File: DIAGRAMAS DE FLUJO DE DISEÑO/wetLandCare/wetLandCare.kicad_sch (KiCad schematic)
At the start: 9 parts, among them M1 Motor_DC, M2 Motor_DC, U1 ESP32-CAM, U2 L298N, U3 AMS1117-5.0, U4 AMS1117-3.3, U5 L298N

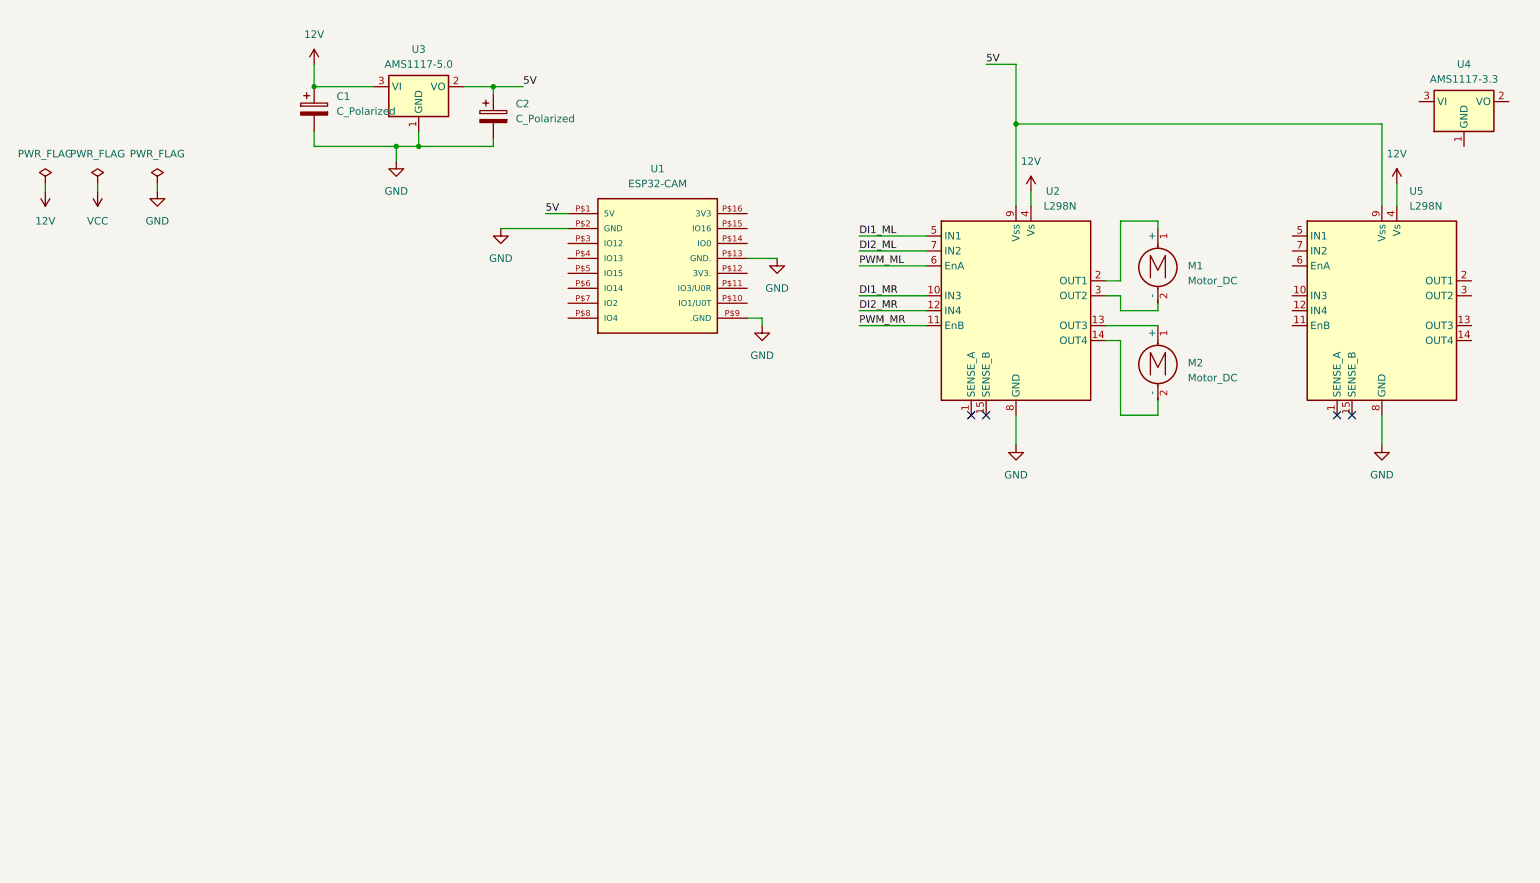
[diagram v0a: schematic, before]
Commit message: Add files via upload
Modificación y complementación del diagrama esquemático como parte del diseño técnico del prototipo
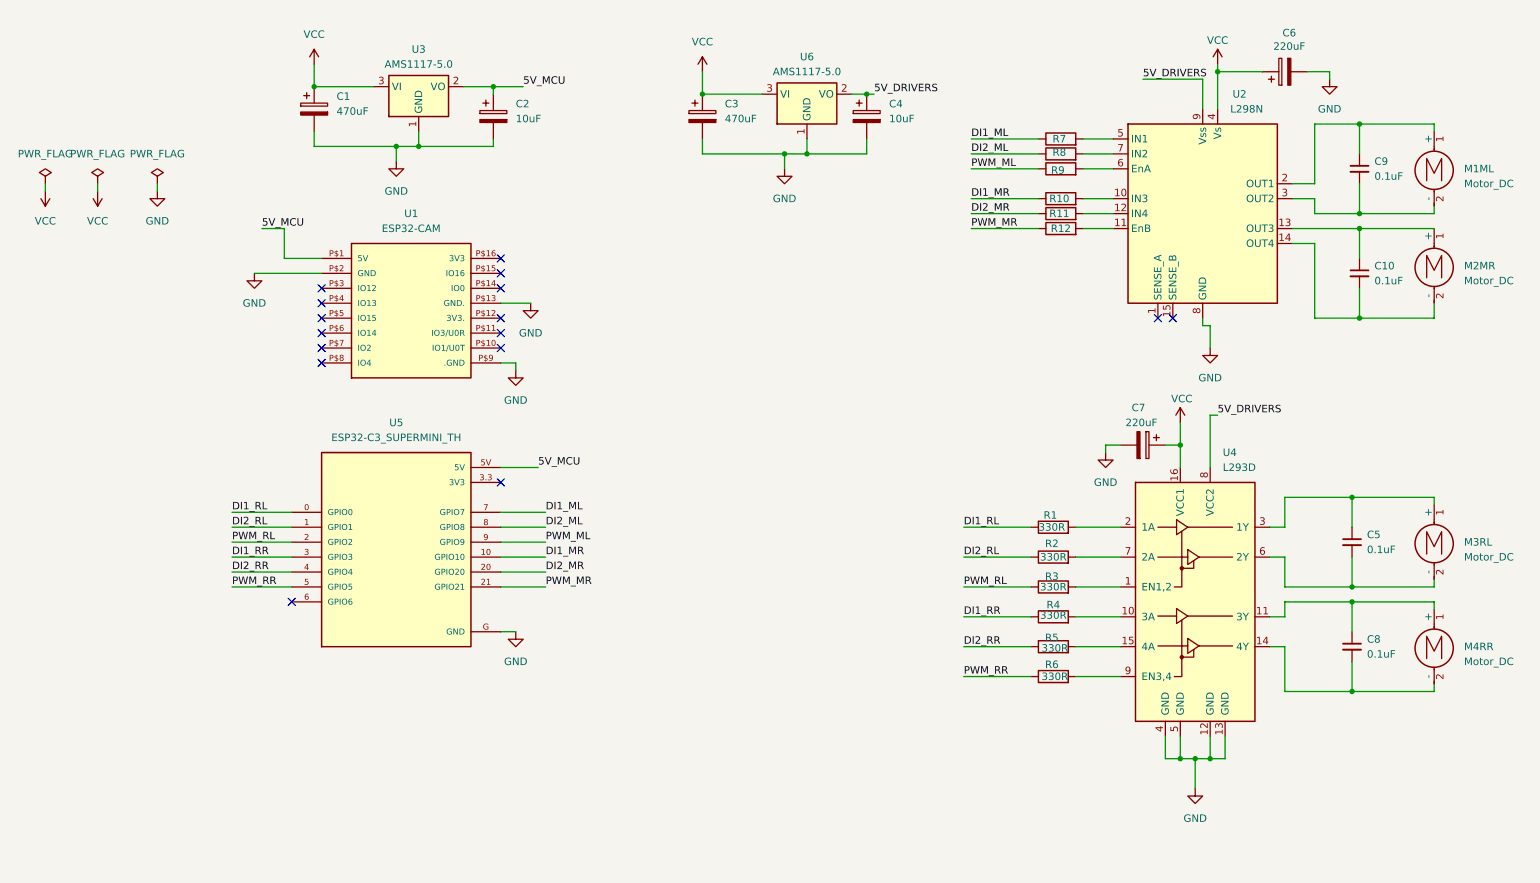
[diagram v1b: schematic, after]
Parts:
- removed U4: AMS1117-3.3, Package_TO_SOT_SMD:SOT-223-3_TabPin2, symbol Regulator_Linear:AMS1117-3.3
- removed U5: L298N, Package_TO_SOT_THT:TO-220-15_P2.54x5.08mm_StaggerOdd_Lead4.58mm_Vertical, symbol Driver_Motor:L298N
- added C10, C5, C8, C9: 0.1uF, symbol Device:C_Small
- added C3: 470uF, symbol Device:C_Polarized
- added C4: 10uF, symbol Device:C_Polarized
- added C6, C7: 220uF, symbol Device:C_Polarized
- added M3RL, M4RR: Motor_DC, symbol Motor:Motor_DC
- added R1, R10, R11, R12, R2, R3, R4, R5, R6, R7, R8, R9: 330R, symbol Device:R
- added U4: L293D, Package_DIP:DIP-16_W7.62mm, symbol Driver_Motor:L293D
- added U5: ESP32-C3_SUPERMINI_TH, ESP32 C3 SuperMini:MODULE_ESP32-C3_SUPERMINI_TH, symbol ESP32-C3_SUPERMINI_TH:ESP32-C3_SUPERMINI_TH
- added U6: AMS1117-5.0, Package_TO_SOT_SMD:SOT-223-3_TabPin2, symbol Regulator_Linear:AMS1117-5.0
- C1: value C_Polarized -> 470uF
- C2: value C_Polarized -> 10uF
- U1: footprint ESP32-CAM:ESP32-CAM -> ESP32CAM:ESP32-CAM
- renumbered M1 to M1ML, M2 to M2MR
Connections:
- net 12V is gone; now on net VCC: C1.1, U2.4 (Vs), U3.3 (VI)
- net DI1_ML: now also R7.1, U5.7 (GPIO7); no longer U2.5 (IN1)
- net DI1_MR: now also R10.1, U5.10 (GPIO10); no longer U2.10 (IN3)
- net DI2_ML: now also R8.1, U5.8 (GPIO8); no longer U2.7 (IN2)
- net DI2_MR: now also R11.1, U5.20 (GPIO20); no longer U2.12 (IN4)
- net GND: now also C3.2, C4.2, C6.2, C7.2, U4.12 (GND), U4.13 (GND), U4.4 (GND), U4.5 (GND), U5.G (GND), U6.1 (GND)
- net PWM_ML: now also R9.1, U5.9 (GPIO9); no longer U2.6 (EnA)
- net PWM_MR: now also R12.1, U5.21 (GPIO21); no longer U2.11 (EnB)
- net VCC: now also C3.1, C6.1, C7.1, U4.16 (VCC1), U6.3 (VI)
- net at M1ML.1 (+), U2.2 (OUT1): now also C9.1
- net at M1ML.2 (-), U2.3 (OUT2): now also C9.2
- net at M2MR.1 (+), U2.13 (OUT3): now also C10.1
- net at M2MR.2 (-), U2.14 (OUT4): now also C10.2
- net 5V renamed 5V_MCU
- net 5V_MCU: now also U5.5V; no longer U2.9 (Vss)
- new net: R6.2, U4.9 (EN3,4)
- new net: R9.2, U2.6 (EnA)
- new net: R3.2, U4.1 (EN1,2)
- new net: R4.2, U4.10 (3A)
- new net: C8.1, M4RR.1 (+), U4.11 (3Y)
- new net: C8.2, M4RR.2 (-), U4.14 (4Y)
- new net: R5.2, U4.15 (4A)
- new net: R1.2, U4.2 (1A)
- new net: C5.1, M3RL.1 (+), U4.3 (1Y)
- new net: C5.2, M3RL.2 (-), U4.6 (2Y)
- new net: R2.2, U4.7 (2A)
- new net: R7.2, U2.5 (IN1)
- new net: R10.2, U2.10 (IN3)
- new net: R11.2, U2.12 (IN4)
- new net: R12.2, U2.11 (EnB)
- new net: R8.2, U2.7 (IN2)
- new net 5V_DRIVERS: C4.1, U2.9 (Vss), U4.8 (VCC2), U6.2 (VO)
- new net DI1_RL: R1.1, U5.0 (GPIO0)
- new net DI1_RR: R4.1, U5.3 (GPIO3)
- new net DI2_RL: R2.1, U5.1 (GPIO1)
- new net DI2_RR: R5.1, U5.4 (GPIO4)
- new net PWM_RL: R3.1, U5.2 (GPIO2)
- new net PWM_RR: R6.1, U5.5 (GPIO5)
- no-connect marks 4 -> 16
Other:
- moved on the sheet: M1ML, M2MR, U1, U2

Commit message: added via upload
Modificaciones al esquemático y diseño del circuito impreso
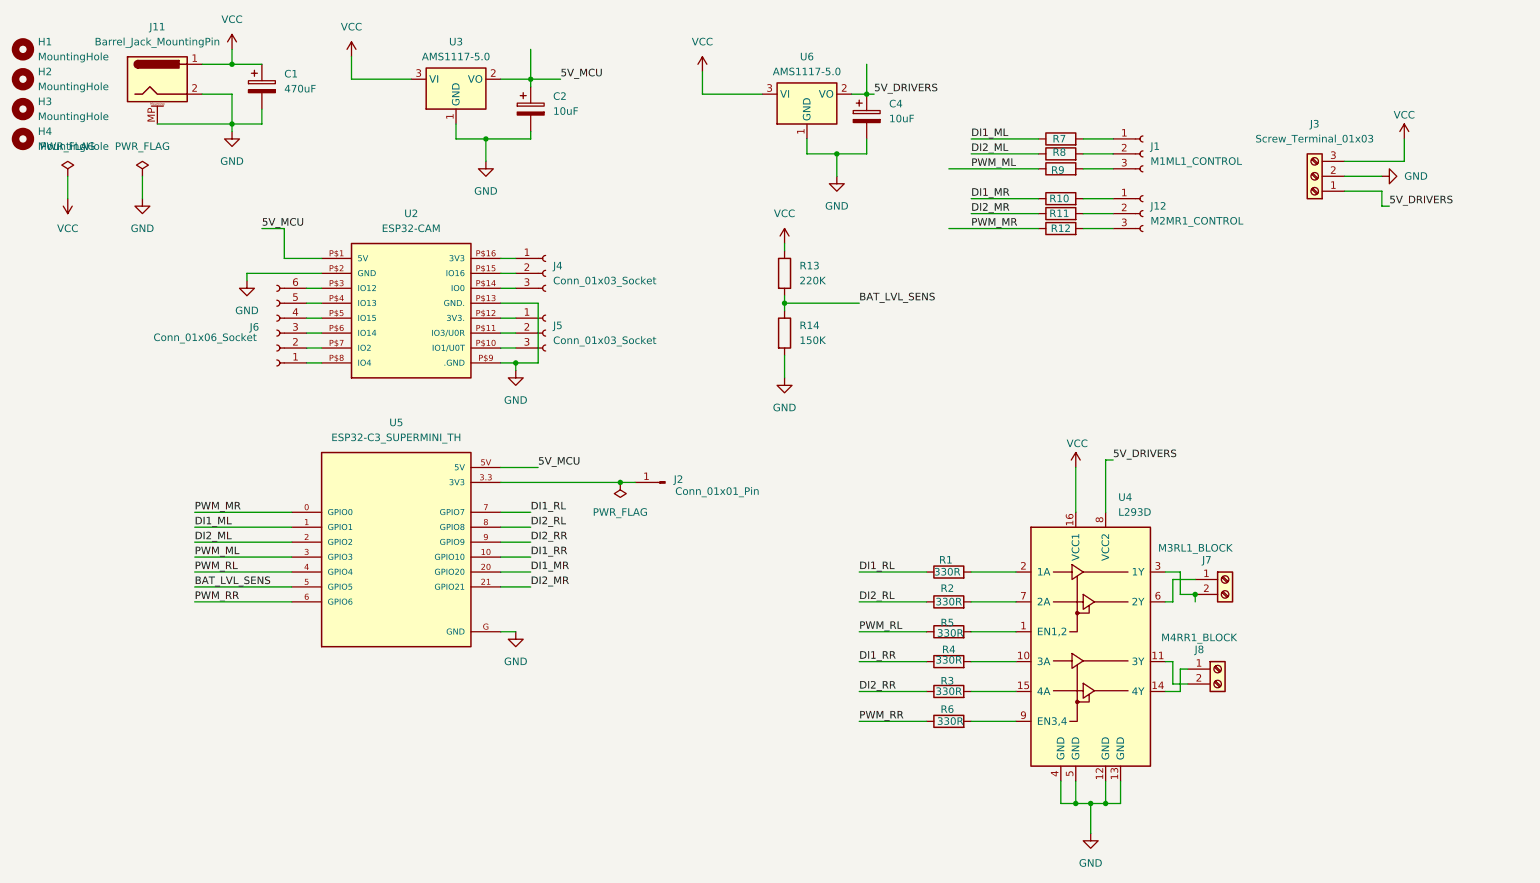
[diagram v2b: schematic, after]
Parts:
- removed C10, C5, C8, C9: 0.1uF, symbol Device:C_Small
- removed C3: 470uF, symbol Device:C_Polarized
- removed C6, C7: 220uF, symbol Device:C_Polarized
- removed M1ML, M2MR, M3RL, M4RR: Motor_DC, symbol Motor:Motor_DC
- removed U1: ESP32-CAM, ESP32CAM:ESP32-CAM, symbol ESP32-CAM:ESP32-CAM
- removed U2: L298N, Package_TO_SOT_THT:TO-220-15_P2.54x5.08mm_StaggerOdd_Lead4.58mm_Vertical, symbol Driver_Motor:L298N
- added H1, H2, H3, H4: MountingHole, MountingHole:MountingHole_3.2mm_M3_DIN965_Pad, symbol Mechanical:MountingHole
- added J1: M1ML1_CONTROL, Connector_PinSocket_2.54mm:PinSocket_1x03_P2.54mm_Vertical, symbol Connector:Conn_01x03_Socket
- added J11: Barrel_Jack_MountingPin, Connector_BarrelJack:BarrelJack_Kycon_KLDX-0202-xC_Horizontal, symbol Connector:Barrel_Jack_MountingPin
- added J12: M2MR1_CONTROL, Connector_PinSocket_2.54mm:PinSocket_1x03_P2.54mm_Vertical, symbol Connector:Conn_01x03_Socket
- added J2: Conn_01x01_Pin, Connector_PinSocket_2.54mm:PinSocket_1x01_P2.54mm_Vertical, symbol Connector:Conn_01x01_Pin
- added J3: Screw_Terminal_01x03, TerminalBlock:TerminalBlock_Altech_AK300-3_P5.00mm, symbol Connector:Screw_Terminal_01x03
- added J4, J5: Conn_01x03_Socket, Connector_PinSocket_2.54mm:PinSocket_1x03_P2.54mm_Vertical, symbol Connector:Conn_01x03_Socket
- added J6: Conn_01x06_Socket, Connector_PinSocket_2.54mm:PinSocket_1x06_P2.54mm_Vertical, symbol Connector:Conn_01x06_Socket
- added J7: M3RL1_BLOCK, TerminalBlock:TerminalBlock_Altech_AK300-2_P5.00mm, symbol Connector:Screw_Terminal_01x02
- added J8: M4RR1_BLOCK, TerminalBlock:TerminalBlock_Altech_AK300-2_P5.00mm, symbol Connector:Screw_Terminal_01x02
- added R13: 220K, Resistor_THT:R_Axial_DIN0207_L6.3mm_D2.5mm_P7.62mm_Horizontal, symbol Device:R
- added R14: 150K, Resistor_THT:R_Axial_DIN0207_L6.3mm_D2.5mm_P7.62mm_Horizontal, symbol Device:R
- added U2: ESP32-CAM, ESP32CAM:ESP32-CAM, symbol ESP32-CAM:ESP32-CAM
- C1: footprint (none) -> Capacitor_THT:CP_Radial_D8.0mm_P3.80mm
- C2, C4: footprint (none) -> Capacitor_THT:CP_Radial_D4.0mm_P2.00mm
- R1, R10, R11, R12, R2, R3, R4, R5, R6, R7, R8, R9: footprint (none) -> Resistor_THT:R_Axial_DIN0207_L6.3mm_D2.5mm_P7.62mm_Horizontal
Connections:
- net 5V_DRIVERS: now also J3.1 (Pin_1)
- net 5V_MCU: now also U2.P$1 (5V)
- net DI1_ML: now also U5.1 (GPIO1); no longer U5.7 (GPIO7)
- net DI1_MR: now also U5.20 (GPIO20); no longer U5.10 (GPIO10)
- net DI1_RL: now also U5.7 (GPIO7); no longer U5.0 (GPIO0)
- net DI1_RR: now also U5.10 (GPIO10); no longer U5.3 (GPIO3)
- net DI2_ML: now also U5.2 (GPIO2); no longer U5.8 (GPIO8)
- net DI2_MR: now also U5.21 (GPIO21); no longer U5.20 (GPIO20)
- net DI2_RL: now also U5.8 (GPIO8); no longer U5.1 (GPIO1)
- net DI2_RR: now also R3.1, U5.9 (GPIO9); no longer R5.1, U5.4 (GPIO4)
- net GND: now also J11.2, J11.MP, J3.2 (Pin_2), R14.2, U2.P$13 (GND.), U2.P$2 (GND), U2.P$9 (.GND)
- net PWM_ML: now also U5.3 (GPIO3); no longer U5.9 (GPIO9)
- net PWM_MR: now also U5.0 (GPIO0); no longer U5.21 (GPIO21)
- net PWM_RL: now also R5.1, U5.4 (GPIO4); no longer R3.1, U5.2 (GPIO2)
- net PWM_RR: now also U5.6 (GPIO6); no longer U5.5 (GPIO5)
- net VCC: now also J11.1, J3.3 (Pin_3), R13.1
- net at R9.2: now also J1.3 (Pin_3)
- net at R3.2: now also U4.15 (4A); no longer U4.1 (EN1,2)
- net at U4.11 (3Y): now also J8.2 (Pin_2)
- net at U4.14 (4Y): now also J8.1 (Pin_1)
- net at R5.2: now also U4.1 (EN1,2); no longer U4.15 (4A)
- net at U4.3 (1Y): now also J7.2 (Pin_2)
- net at U4.6 (2Y): now also J7.1 (Pin_1)
- net at R7.2: now also J1.1 (Pin_1)
- net at R10.2: now also J12.1 (Pin_1)
- net at R11.2: now also J12.2 (Pin_2)
- net at R12.2: now also J12.3 (Pin_3)
- net at R8.2: now also J1.2 (Pin_2)
- net at U5.3.3 (3V3): now also J2.1 (Pin_1)
- new net: J5.1 (Pin_1), U2.P$12 (3V3.)
- new net: J5.2 (Pin_2), U2.P$11 (IO3/U0R)
- new net: J5.3 (Pin_3), U2.P$10 (IO1/U0T)
- new net: J6.1 (Pin_1), U2.P$8 (IO4)
- new net: J6.2 (Pin_2), U2.P$7 (IO2)
- new net: J6.3 (Pin_3), U2.P$6 (IO14)
- new net: J6.4 (Pin_4), U2.P$5 (IO15)
- new net: J6.5 (Pin_5), U2.P$4 (IO13)
- new net: J6.6 (Pin_6), U2.P$3 (IO12)
- new net: J4.1 (Pin_1), U2.P$16 (3V3)
- new net: J4.2 (Pin_2), U2.P$15 (IO16)
- new net: J4.3 (Pin_3), U2.P$14 (IO0)
- new net BAT_LVL_SENS: R13.2, R14.1, U5.5 (GPIO5)
- no-connect marks 16 -> 0
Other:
- moved on the sheet: C1, C2, R1, R2, R3, R4, R5, R6, U3, U4

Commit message: updated kicad files
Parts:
- removed J7: M3RL1_BLOCK, TerminalBlock:TerminalBlock_Altech_AK300-2_P5.00mm, symbol Connector:Screw_Terminal_01x02
- removed J8: M4RR1_BLOCK, TerminalBlock:TerminalBlock_Altech_AK300-2_P5.00mm, symbol Connector:Screw_Terminal_01x02
- added J9: Screw_Terminal_01x04, TerminalBlock:TerminalBlock_Altech_AK300-4_P5.00mm, symbol Connector:Screw_Terminal_01x04
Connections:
- net BAT_LVL_SENS: now also U5.0 (GPIO0); no longer U5.5 (GPIO5)
- net PWM_MR: now also U5.5 (GPIO5); no longer U5.0 (GPIO0)
- net at U4.11 (3Y): now also J9.2 (Pin_2)
- net at U4.14 (4Y): now also J9.1 (Pin_1)
- net at U4.3 (1Y): now also J9.4 (Pin_4)
- net at U4.6 (2Y): now also J9.3 (Pin_3)
